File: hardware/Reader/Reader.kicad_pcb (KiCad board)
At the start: 4 copper layers, 135 parts, among them CN1 AHDF15A-KG-TAXB

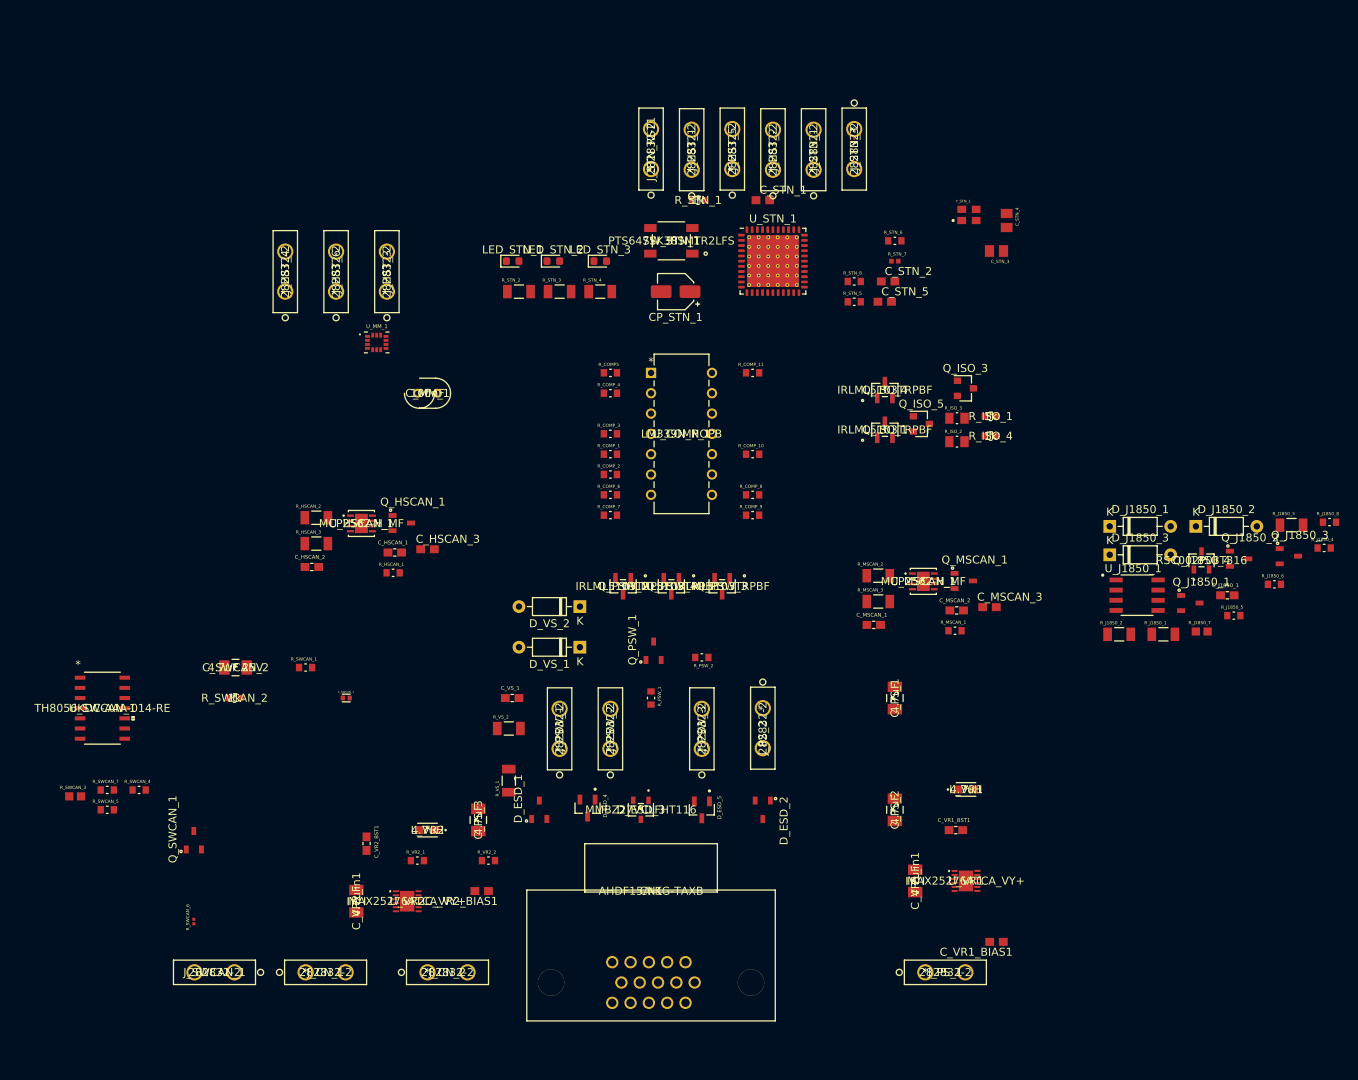
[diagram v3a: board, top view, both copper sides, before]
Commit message: Fixed bugs on the reader schematic. Exported Schematic Electrical report
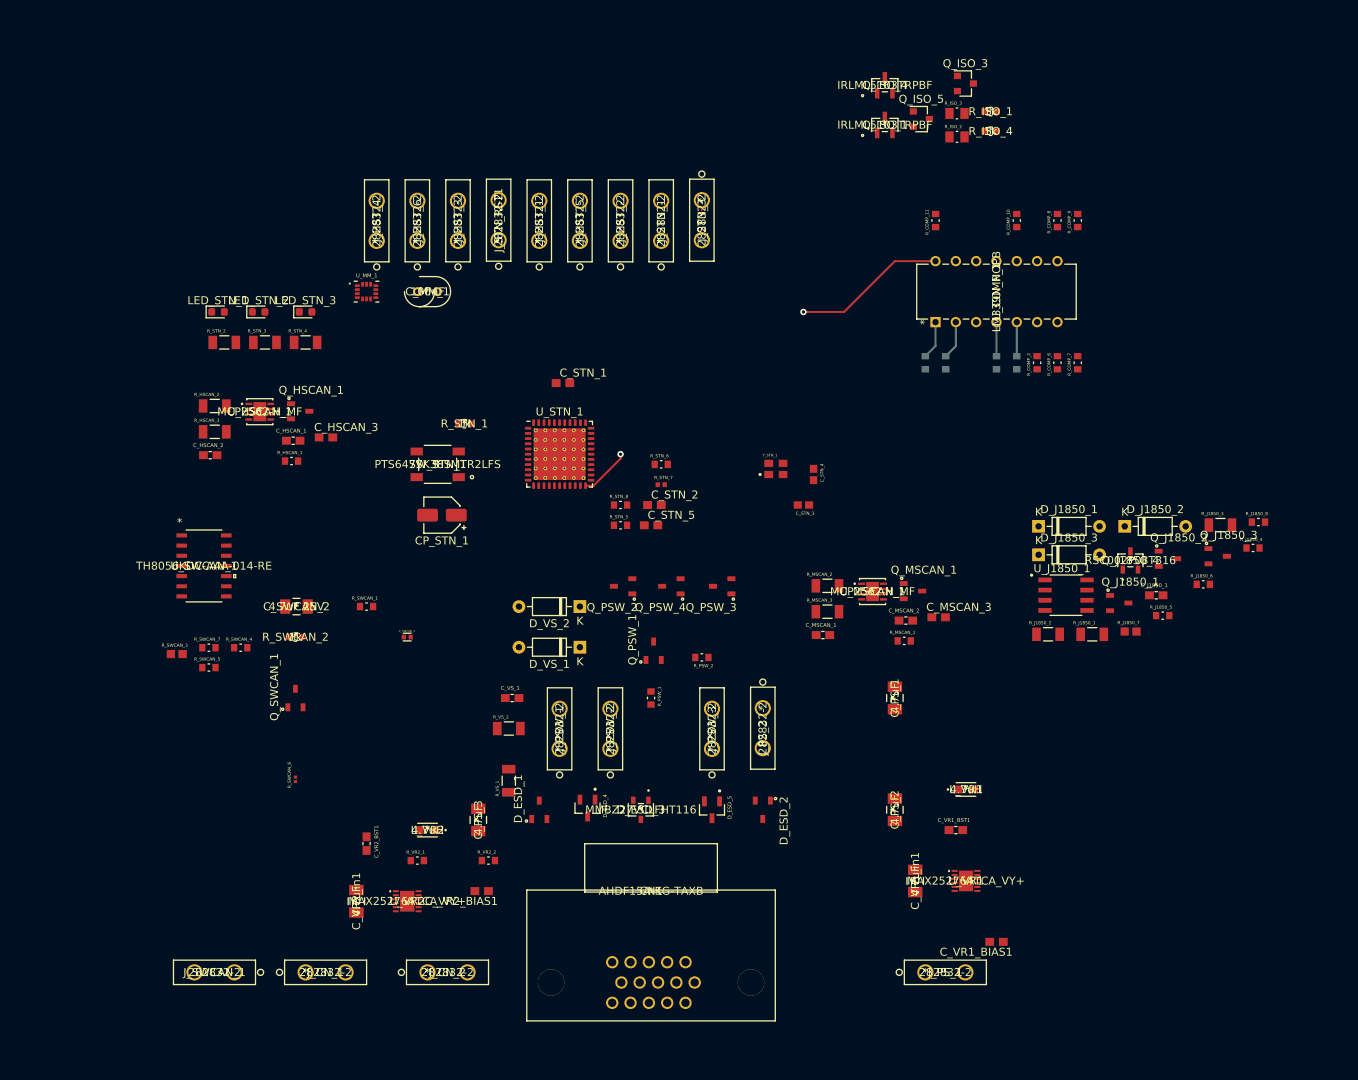
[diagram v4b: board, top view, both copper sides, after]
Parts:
- C_STN_3, C_STN_4: footprint footprints:CAPC2012X88N -> footprints:CAPC1608X90N
- Q_PSW_2, Q_PSW_3, Q_PSW_4: value IRLML5103TRPBF -> NX7002AK,215; footprint footprints:IRLML5103TRPBF -> footprints:SOT95P230X110-3N
- R_COMP5, R_COMP_1, R_COMP_3, R_COMP_4: moved to B.Cu
- moved R_COMP_7 61.4 mm to (193.0, 71.1), turned to 90 degrees
- moved R_COMP_6 58.3 mm to (190.5, 71.1), turned to 90 degrees
- moved R_COMP_2 55.1 mm to (188.0, 71.1), turned to 90 degrees
- moved R_COMP_9 54.8 mm to (193.0, 53.3), turned to 90 degrees
- moved R_COMP_1 52.1 mm to (185.4, 71.1), turned to 90 degrees
- moved R_COMP_8 51.3 mm to (190.5, 53.3), turned to 90 degrees
- moved R_COMP_3 49.1 mm to (182.9, 71.1), turned to 270 degrees
- moved R_COMP_10 44.1 mm to (185.4, 53.3), turned to 90 degrees
- moved R_COMP_4 42.1 mm to (176.5, 71.1), turned to 90 degrees
- moved CP_STN_1 40.4 mm to (113.6, 90.2)
- moved C_STN_2 40.4 mm to (140.1, 88.9)
- moved R_STN_8 40.4 mm to (135.9, 88.9)
- moved C_STN_5 40.4 mm to (139.7, 91.4)
- moved R_STN_1 40.4 mm to (116.4, 78.7)
- moved R_STN_5 40.4 mm to (135.9, 91.4)
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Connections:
- J_PS_1 pad 2: Pin16_Raw_+12V_Battery -> /OBDII Interpreter/Analog_Voltage
- Q_J1850_2 pad 3: /OBDII Interpreter/J1850_BUS- -> Pin10_SAE_J1850_BUS-
- Q_MSCAN_1 pad 1: /OBDII Interpreter/Medium Speed CAN Transceiver/~PWR_CTRL~ -> /OBDII Interpreter/~PWR_CTRL~
- R_COMP_3 pad 2: /OBDII Interpreter/J1850_BUS- -> Pin10_SAE_J1850_BUS-
- R_J1850_5 pad 2: /OBDII Interpreter/J1850_BUS- -> Pin10_SAE_J1850_BUS-
- U_J1850_1 pad 3: +V_J1850 -> Net-(U_J1850_1-Pad3)
- U_J1850_1 pad 6: +V_J1850 -> Net-(U_J1850_1-Pad6)
- U_J1850_1 pad 7: +V_J1850 -> Net-(U_J1850_1-Pad7)
- U_J1850_1 pad 8: Net-(U_J1850_1-Pad5) -> Net-(U_J1850_1-Pad8)
- U_STN_1 pad 21: /OBDII Interpreter/OBDII Chip/~ISO_RX~ -> /OBDII Interpreter/Comparator Transceiver/~ISO_RX~
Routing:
- net /OBDII Interpreter/Comparator Transceiver/VPW_RX: track 0.00 -> 55.7 mm, vias 0 -> 2
- net /OBDII Interpreter/Comparator Transceiver/PWM_RX: track 0.00 -> 4.79 mm
- net /OBDII Interpreter/Comparator Transceiver/~ISO_RX~: track 0.00 -> 4.79 mm
- net Net-(R_COMP_3-Pad1): track 0.00 -> 4.26 mm
- net Net-(R_COMP_1-Pad2): track 0.00 -> 4.26 mm

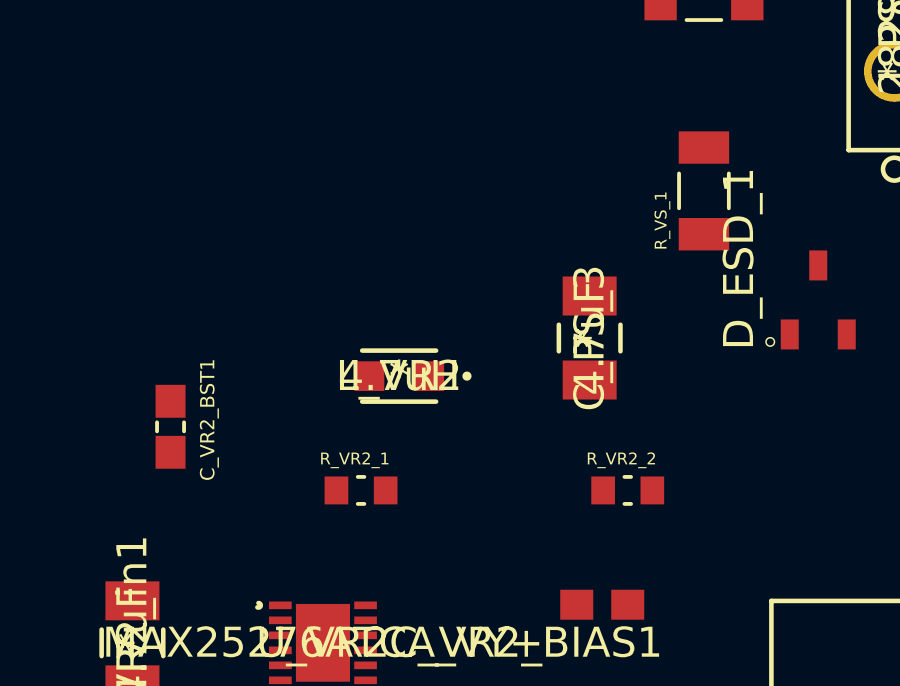
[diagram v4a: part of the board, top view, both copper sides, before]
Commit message: Changed resistor divider for VR2 for cheaper resistors
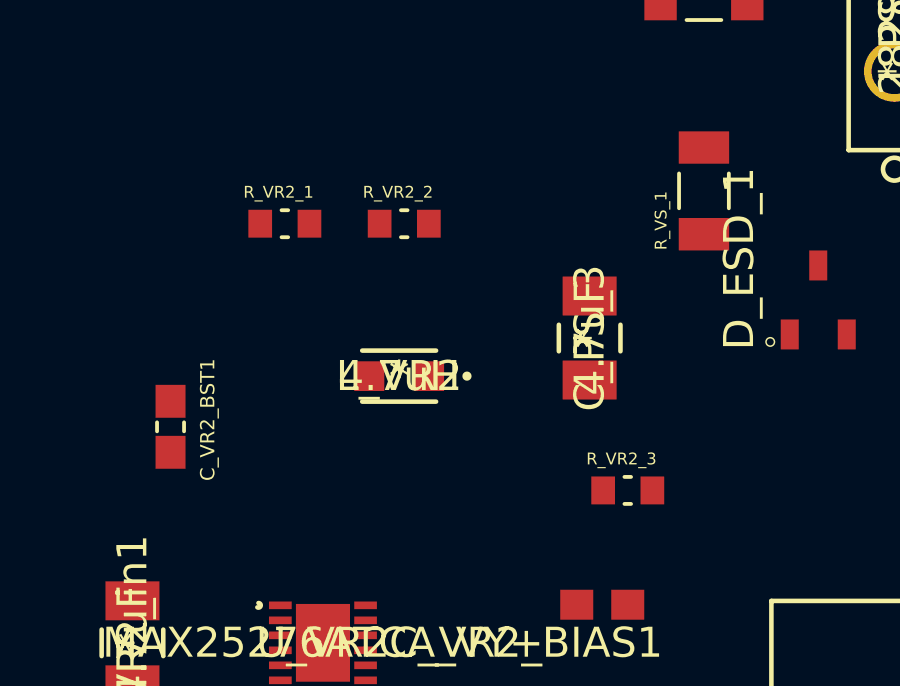
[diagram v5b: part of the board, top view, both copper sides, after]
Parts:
- added R_VR2_2: 100k, footprints:RESC1608X55N, F.Cu at (111.9, 124.5)
- R_VR2_1: value 50k -> 100k
- moved R_VR2_1 9.25 mm to (108.0, 124.5)
- renumbered R_VR2_2 to R_VR2_3
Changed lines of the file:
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@@
     (tracks 19)
     (zones 0)
-    (modules 135)
+    (modules 136)
     (nets 119)
   )
@@
     (add_net VDDA)
   )
+  (module footprints:RESC1608X55N (layer F.Cu)
+    (at 111.93 124.46)
+    (fp_text reference R_VR2_2 (at -0.21 -1.05) (layer F.SilkS)
+      (effects (font (size 0.393701 0.393701) (thickness 0.015)))
+    )
+    (fp_text value 100k (at 1.54 1.05) (layer F.Fab)
+      (effects (font (size 0.393701 0.393701) (thickness 0.015)))
+    )
+    (fp_line (start 0.85 0.45) (end -0.85 0.45) (layer F.Fab) (width 0.127))
+    (fp_line (start 0.85 -0.45) (end -0.85 -0.45) (layer F.Fab) (width 0.127))
+    (fp_line (start 0.85 0.45) (end 0.85 -0.45) (layer F.Fab) (width 0.127))
+    (fp_line (start -0.85 0.45) (end -0.85 -0.45) (layer F.Fab) (width 0.127))
+    (fp_line (start -0.11 -0.45) (end 0.11 -0.45) (layer F.SilkS) (width 0.127))
+    (fp_line (start -0.11 0.45) (end 0.11 0.45) (layer F.SilkS) (width 0.127))
+    (fp_line (start -1.465 0.715) (end 1.465 0.715) (layer F.CrtYd) (width 0.05))
+    (fp_line (start -1.465 -0.715) (end 1.465 -0.715) (layer F.CrtYd) (width 0.05))
+    (fp_line (start -1.465 0.715) (end -1.465 -0.715) (layer F.CrtYd) (width 0.05))
+    (fp_line (start 1.465 0.715) (end 1.465 -0.715) (layer F.CrtYd) (width 0.05))
+    (pad 2 smd rect (at 0.82 0) (size 0.79 0.93) (layers F.Cu F.Paste F.Mask)
+      (net 1 Pin4_GnD_Chassis))
+    (pad 1 smd rect (at -0.82 0) (size 0.79 0.93) (layers F.Cu F.Paste F.Mask)
+      (net 64 "Net-(R_VR2_1-Pad2)"))
+  )
+  (module footprints:RESC1608X55N (layer F.Cu)
+    (at 107.95 124.46)
+    (fp_text reference R_VR2_1 (at -0.21 -1.05) (layer F.SilkS)
+      (effects (font (size 0.393701 0.393701) (thickness 0.015)))
+    )
+    (fp_text value 100k (at 1.54 1.05) (layer F.Fab)
+      (effects (font (size 0.393701 0.393701) (thickness 0.015)))
+    )
+    (fp_line (start 0.85 0.45) (end -0.85 0.45) (layer F.Fab) (width 0.127))
+    (fp_line (start 0.85 -0.45) (end -0.85 -0.45) (layer F.Fab) (width 0.127))
+    (fp_line (start 0.85 0.45) (end 0.85 -0.45) (layer F.Fab) (width 0.127))
+    (fp_line (start -0.85 0.45) (end -0.85 -0.45) (layer F.Fab) (width 0.127))
+    (fp_line (start -0.11 -0.45) (end 0.11 -0.45) (layer F.SilkS) (width 0.127))
+    (fp_line (start -0.11 0.45) (end 0.11 0.45) (layer F.SilkS) (width 0.127))
+    (fp_line (start -1.465 0.715) (end 1.465 0.715) (layer F.CrtYd) (width 0.05))
+    (fp_line (start -1.465 -0.715) (end 1.465 -0.715) (layer F.CrtYd) (width 0.05))
+    (fp_line (start -1.465 0.715) (end -1.465 -0.715) (layer F.CrtYd) (width 0.05))
+    (fp_line (start 1.465 0.715) (end 1.465 -0.715) (layer F.CrtYd) (width 0.05))
+    (pad 2 smd rect (at 0.82 0) (size 0.79 0.93) (layers F.Cu F.Paste F.Mask)
+      (net 64 "Net-(R_VR2_1-Pad2)"))
+    (pad 1 smd rect (at -0.82 0) (size 0.79 0.93) (layers F.Cu F.Paste F.Mask)
+      (net 1 Pin4_GnD_Chassis))
+  )
   (module footprints:SOT95P237X111-3N (layer F.Cu)
     (at 147.32 127 270)
@@
   )
   (module footprints:RESC1608X55N (layer F.Cu)
-    (at 110.49 133.35)
-    (fp_text reference R_VR2_1 (at -0.21 -1.05) (layer F.SilkS)
-      (effects (font (size 0.393701 0.393701) (thickness 0.015)))
-    )
-    (fp_text value 50k (at 1.54 1.05) (layer F.Fab)
-      (effects (font (size 0.393701 0.393701) (thickness 0.015)))
-    )
-    (fp_line (start 0.85 0.45) (end -0.85 0.45) (layer F.Fab) (width 0.127))
-    (fp_line (start 0.85 -0.45) (end -0.85 -0.45) (layer F.Fab) (width 0.127))
-    (fp_line (start 0.85 0.45) (end 0.85 -0.45) (layer F.Fab) (width 0.127))
-    (fp_line (start -0.85 0.45) (end -0.85 -0.45) (layer F.Fab) (width 0.127))
-    (fp_line (start -0.11 -0.45) (end 0.11 -0.45) (layer F.SilkS) (width 0.127))
-    (fp_line (start -0.11 0.45) (end 0.11 0.45) (layer F.SilkS) (width 0.127))
-    (fp_line (start -1.465 0.715) (end 1.465 0.715) (layer F.CrtYd) (width 0.05))
-    (fp_line (start -1.465 -0.715) (end 1.465 -0.715) (layer F.CrtYd) (width 0.05))
-    (fp_line (start -1.465 0.715) (end -1.465 -0.715) (layer F.CrtYd) (width 0.05))
-    (fp_line (start 1.465 0.715) (end 1.465 -0.715) (layer F.CrtYd) (width 0.05))
-    (pad 1 smd rect (at -0.82 0) (size 0.79 0.93) (layers F.Cu F.Paste F.Mask)
-      (net 1 Pin4_GnD_Chassis))
-    (pad 2 smd rect (at 0.82 0) (size 0.79 0.93) (layers F.Cu F.Paste F.Mask)
-      (net 64 "Net-(R_VR2_1-Pad2)"))
-  )
-  (module footprints:RESC1608X55N (layer F.Cu)
     (at 119.38 133.35)
-    (fp_text reference R_VR2_2 (at -0.21 -1.05) (layer F.SilkS)
+    (fp_text reference R_VR2_3 (at -0.21 -1.05) (layer F.SilkS)
       (effects (font (size 0.393701 0.393701) (thickness 0.015)))
     )
